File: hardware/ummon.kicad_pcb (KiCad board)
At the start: 4 copper layers, 140 x 83.5 mm, 85 parts, among them J1 Conn_01x08_Pin, J2 Conn_01x05_Pin, J3 Conn_01x04_Pin, J4 Conn_01x04_Pin, J5 Conn_01x04_Pin, P1 FPC 0.5MM 24P Vertical, Q1 SI1308EDL, SW1 Reboot, SW2 Flash, SW3 Test Button, U1 ESP32-C6-WROOM-1-N8, U2 SCD41-D-R2, U3 SGP41-D-R4, U4 SHT41-AD1B-R2, U5 AMS1117-3.3, U7 SMBJ6.5CA

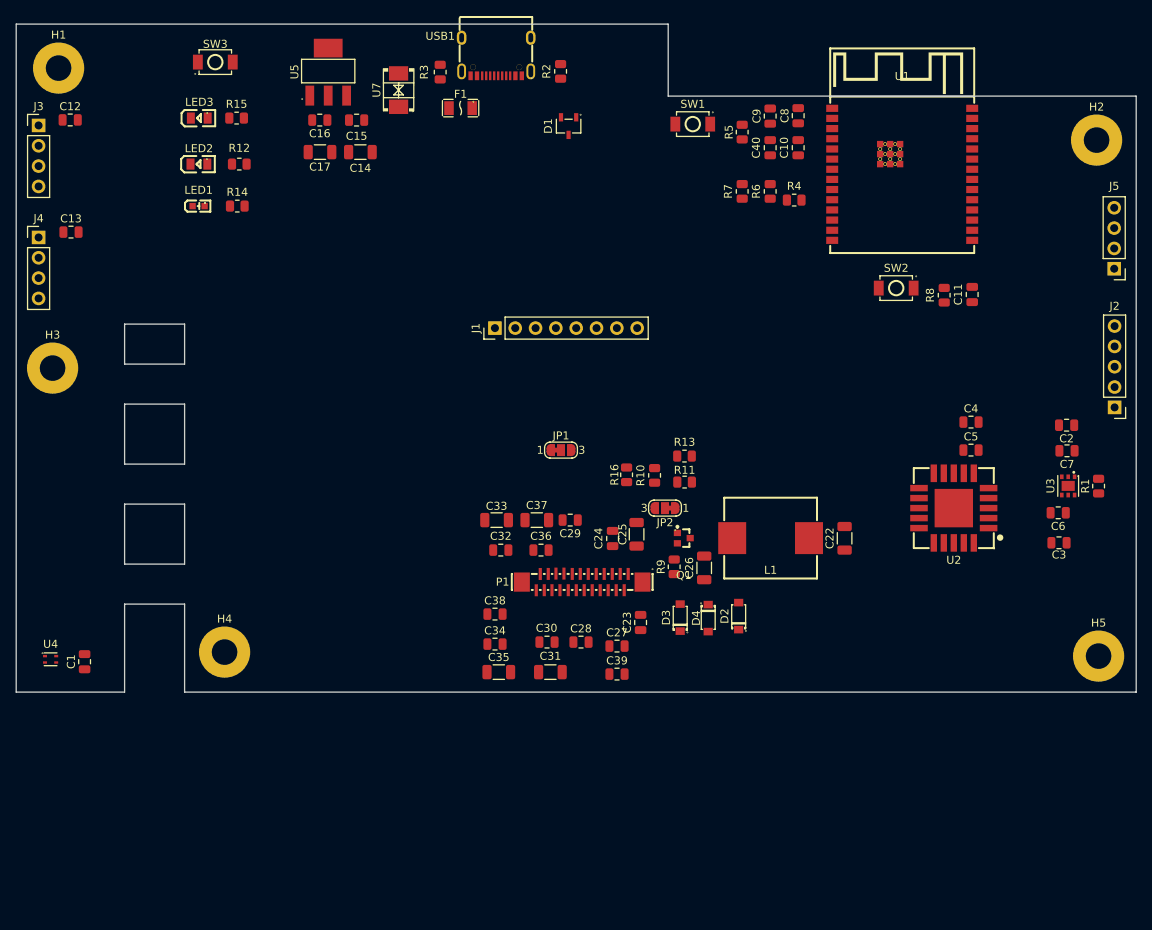
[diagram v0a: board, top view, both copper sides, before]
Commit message: :recycle: Propper outline of pcb and rearangement
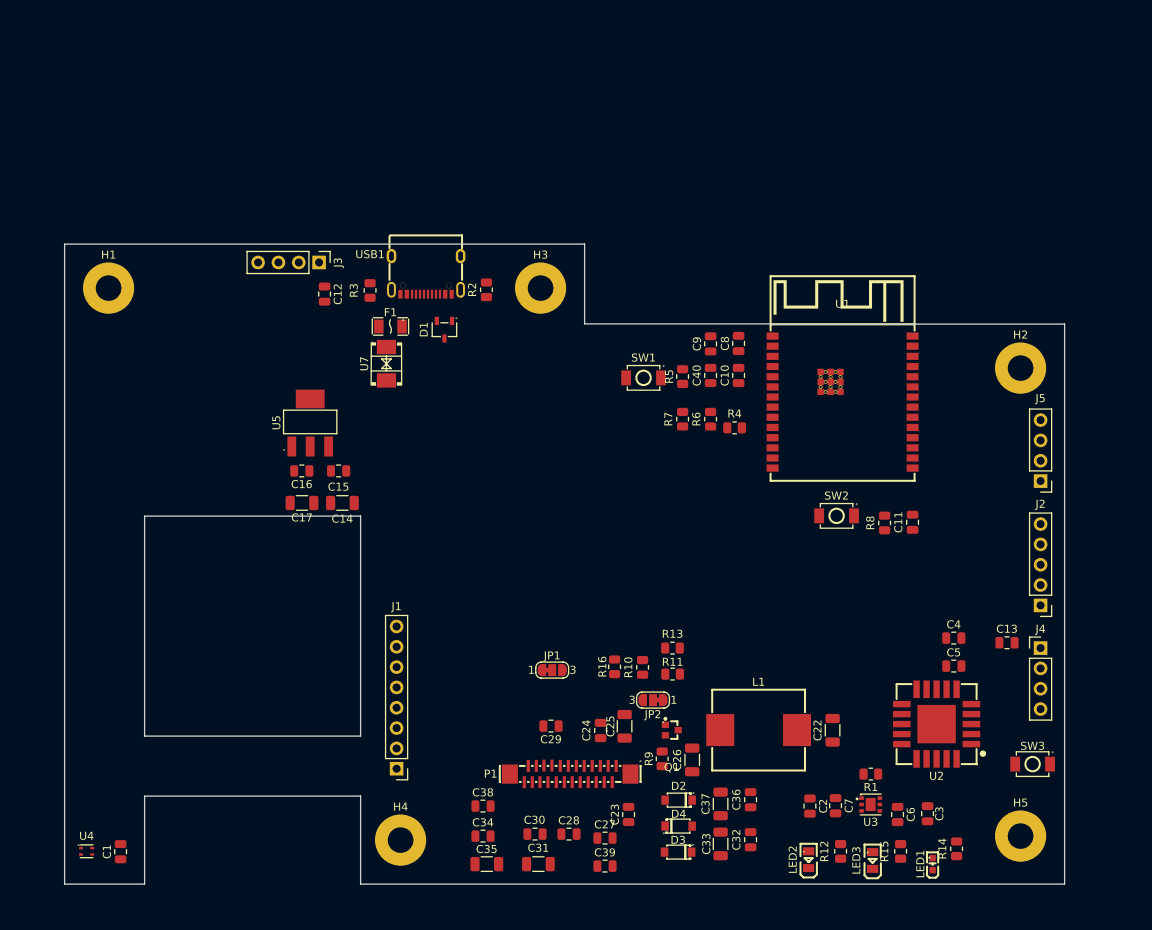
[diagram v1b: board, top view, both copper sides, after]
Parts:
- moved J4 135.4 mm to (172.0, 120.5)
- moved SW3 134.7 mm to (171.0, 135.0), turned to 0 degrees
- moved C13 127.8 mm to (167.8, 119.8), turned to 180 degrees
- moved LED3 125.3 mm to (151.0, 147.1), turned to 90 degrees
- moved R15 123.7 mm to (154.5, 145.9), turned to 90 degrees
- moved LED1 123.2 mm to (158.5, 147.5), turned to 90 degrees
- moved R14 120.6 mm to (161.5, 145.6), turned to -90 degrees
- moved LED2 115.6 mm to (143.0, 146.9), turned to 90 degrees
- moved R12 114.2 mm to (147.0, 145.9), turned to 90 degrees
- moved H3 61.8 mm to (109.5, 75.5)
- moved C2 57.4 mm to (143.2, 140.2), turned to -90 degrees
- moved J1 56.4 mm to (91.5, 135.6), turned to 180 degrees
- moved C7 53.0 mm to (146.4, 140.2), turned to -90 degrees
- moved C33 49.2 mm to (132.0, 145.0), turned to -90 degrees
- moved C32 47.8 mm to (135.8, 144.4), turned to -90 degrees
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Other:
- board size 140 x 83.5 mm -> 125 x 80 mm

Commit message: :sparkles: Rounding of pcb edges
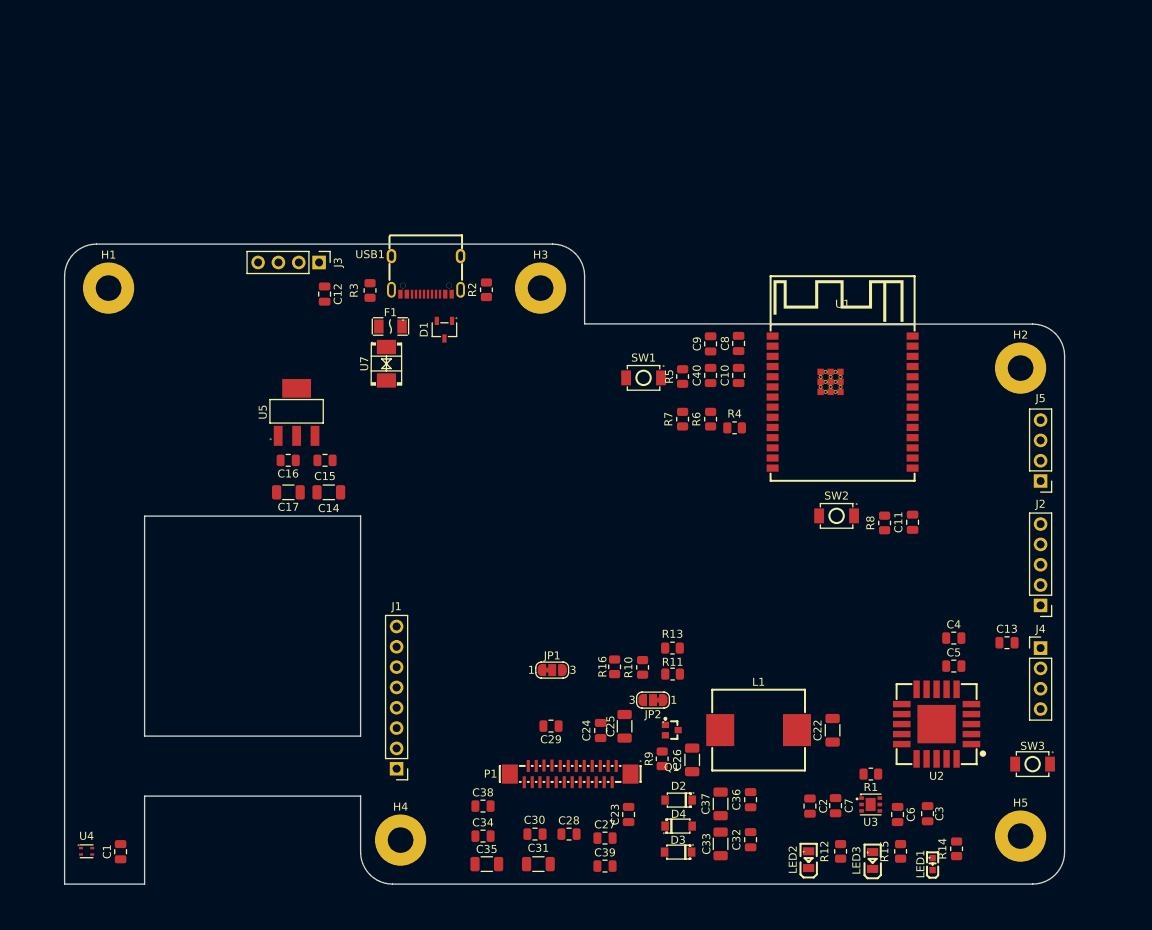
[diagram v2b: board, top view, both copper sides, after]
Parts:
- moved C15 2.16 mm to (82.5, 97.0)
- moved C16 2.16 mm to (78.0, 97.0)
- moved C17 2.16 mm to (78.0, 101.0)
- moved U5 2.16 mm to (79.0, 91.0)
- moved C14 2.16 mm to (83.0, 101.0)
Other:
- outline, holes or cut-outs redrawn
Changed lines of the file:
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@@
 	(footprint "Capacitor_SMD:C_0805_2012Metric"
 		(layer "F.Cu")
-		(at 79.65 98.3575 180)
+		(at 77.95 97.03 180)
 		(descr "Capacitor SMD 0805 (2012 Metric), square (rectangular) end terminal, IPC-7351 nominal, (Body size source: IPC-SM-782 page 76, https://www.pcb-3d.com/wordpress/wp-content/uploads/ipc-sm-782a_amendment_1_and_2.pdf, https://docs.google.com/spreadsheets/d/1BsfQQcO9C6DZCsRaXUlFlo91Tg2WpOkGARC1WS5S8t0/edit?usp=sharing)")
 		(tags "capacitor")
@@
 	(footprint "Capacitor_SMD:C_0805_2012Metric"
 		(layer "F.Cu")
-		(at 84.25 98.3575)
+		(at 82.55 97.03)
 		(descr "Capacitor SMD 0805 (2012 Metric), square (rectangular) end terminal, IPC-7351 nominal, (Body size source: IPC-SM-782 page 76, https://www.pcb-3d.com/wordpress/wp-content/uploads/ipc-sm-782a_amendment_1_and_2.pdf, https://docs.google.com/spreadsheets/d/1BsfQQcO9C6DZCsRaXUlFlo91Tg2WpOkGARC1WS5S8t0/edit?usp=sharing)")
 		(tags "capacitor")
@@
 	(footprint "parts:SOT-223-3_L6.5-W3.4-P2.30-LS7.0-BR"
 		(layer "F.Cu")
-		(at 80.7 92.3275 -90)
+		(at 79 91 -90)
 		(property "Reference" "U5"
 			(at 0 4.2 90)
@@
 	(footprint "Capacitor_SMD:C_1206_3216Metric"
 		(layer "F.Cu")
-		(at 84.725 102.3575)
+		(at 83.025 101.03)
 		(descr "Capacitor SMD 1206 (3216 Metric), square (rectangular) end terminal, IPC-7351 nominal, (Body size source: IPC-SM-782 page 76, https://www.pcb-3d.com/wordpress/wp-content/uploads/ipc-sm-782a_amendment_1_and_2.pdf)")
 		(tags "capacitor")
@@
 	(footprint "Capacitor_SMD:C_1206_3216Metric"
 		(layer "F.Cu")
-		(at 79.675 102.3575 180)
+		(at 77.975 101.03 180)
 		(descr "Capacitor SMD 1206 (3216 Metric), square (rectangular) end terminal, IPC-7351 nominal, (Body size source: IPC-SM-782 page 76, https://www.pcb-3d.com/wordpress/wp-content/uploads/ipc-sm-782a_amendment_1_and_2.pdf)")
 		(tags "capacitor")
@@
 		)
 	)
+	(gr_arc
+		(start 50 74)
+		(mid 51.171573 71.171573)
+		(end 54 70)
+		(stroke
+			(width 0.05)
+			(type default)
+		)
+		(layer "Edge.Cuts")
+	)
 	(gr_line
 		(start 50 150)
-		(end 50 70)
+		(end 50 74)
 		(stroke
 			(width 0.05)
@@
 	)
 	(gr_line
-		(start 87 150)
+		(start 87 146)
 		(end 87 139)
 		(stroke
@@
 		(layer "Edge.Cuts")
 	)
+	(gr_arc
+		(start 91 150)
+		(mid 88.171573 148.828427)
+		(end 87 146)
+		(stroke
+			(width 0.05)
+			(type default)
+		)
+		(layer "Edge.Cuts")
+	)
 	(gr_line
-		(start 87 150)
-		(end 175 150)
+		(start 91 150)
+		(end 171 150)
 		(stroke
 			(width 0.05)
@@
 	)
 	(gr_line
-		(start 115 70)
-		(end 50 70)
+		(start 111 70)
+		(end 54 70)
+		(stroke
+			(width 0.05)
+			(type default)
+		)
+		(layer "Edge.Cuts")
+	)
+	(gr_arc
+		(start 111 70)
+		(mid 113.828427 71.171573)
+		(end 115 74)
 		(stroke
 			(width 0.05)
@@
 	(gr_line
 		(start 115 79.97)
-		(end 115 70)
+		(end 115 74)
 		(stroke
 			(width 0.05)
@@
 	)
 	(gr_line
-		(start 175 80)
+		(start 171.002 79.998001)
 		(end 115 79.97)
 		(stroke
@@
 		(layer "Edge.Cuts")
 	)
+	(gr_arc
+		(start 171.002 79.998001)
+		(mid 173.829134 81.17028)
+		(end 175 83.998)
+		(stroke
+			(width 0.05)
+			(type default)
+		)
+		(layer "Edge.Cuts")
+	)
+	(gr_arc
+		(start 175 146)
+		(mid 173.828427 148.828427)
+		(end 171 150)
+		(stroke
+			(width 0.05)
+			(type default)
+		)
+		(layer "Edge.Cuts")
+	)
 	(gr_line
-		(start 175 150)
-		(end 175 80)
+		(start 175 146)
+		(end 175 83.998)
 		(stroke
 			(width 0.05)

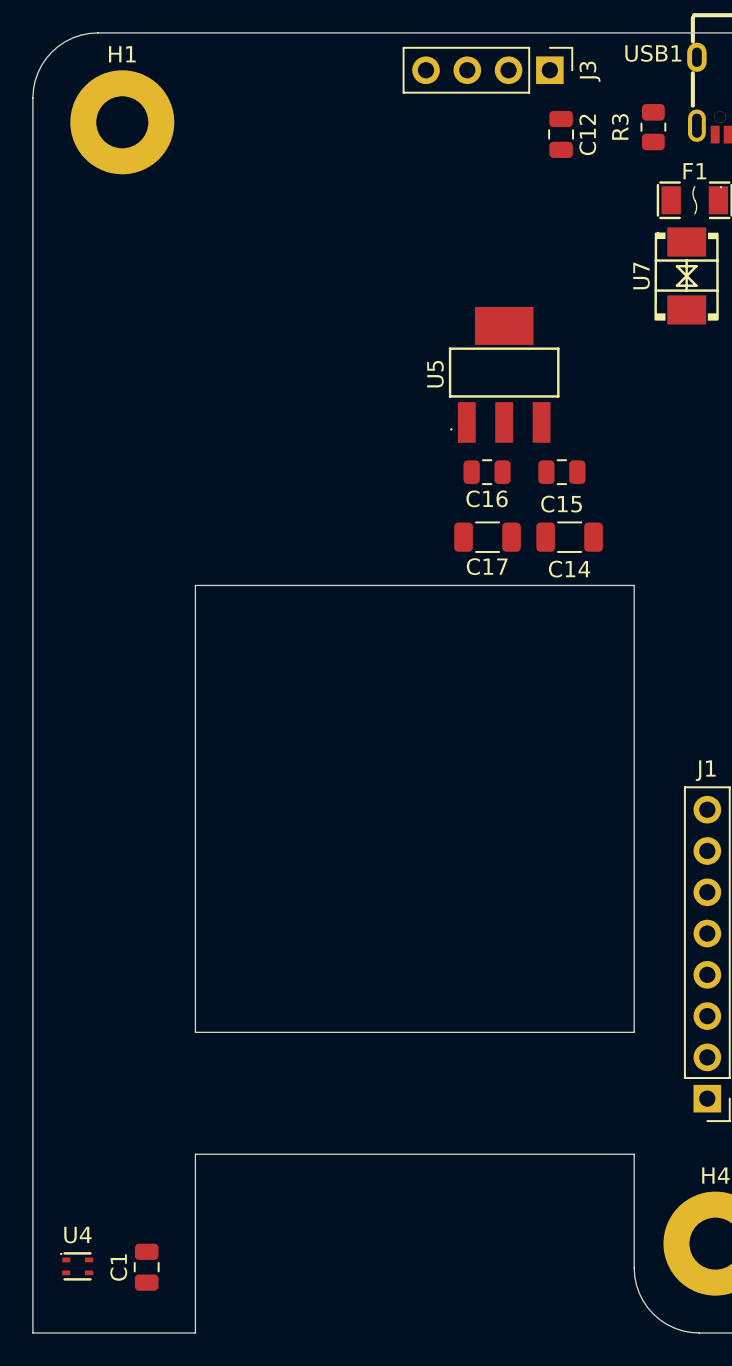
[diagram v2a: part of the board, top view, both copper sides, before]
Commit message: :sparkles: Add extra mounting hole for pcb sht41 part
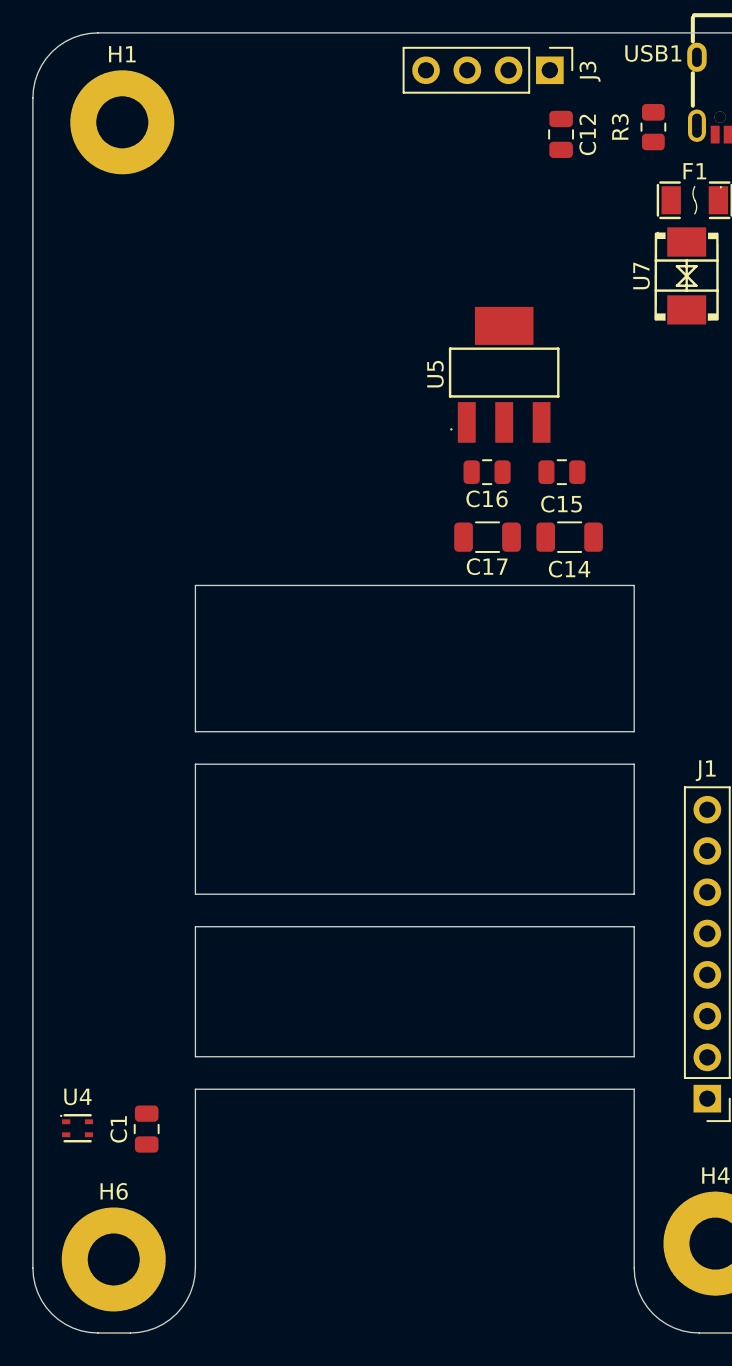
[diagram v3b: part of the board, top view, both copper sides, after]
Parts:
- added H6: MountingHole_Pad, MountingHole:MountingHole_3.2mm_M3_Pad, F.Cu at (55.0, 145.5)
- moved C1 8.50 mm to (57.0, 137.4)
- moved U4 8.50 mm to (52.8, 137.4)
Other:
- outline, holes or cut-outs redrawn
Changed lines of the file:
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@@
 	(footprint "Capacitor_SMD:C_0805_2012Metric"
 		(layer "F.Cu")
-		(at 57 145.95 90)
+		(at 57 137.45 90)
 		(descr "Capacitor SMD 0805 (2012 Metric), square (rectangular) end terminal, IPC-7351 nominal, (Body size source: IPC-SM-782 page 76, https://www.pcb-3d.com/wordpress/wp-content/uploads/ipc-sm-782a_amendment_1_and_2.pdf, https://docs.google.com/spreadsheets/d/1BsfQQcO9C6DZCsRaXUlFlo91Tg2WpOkGARC1WS5S8t0/edit?usp=sharing)")
 		(tags "capacitor")
@@
 	(footprint "parts:DFN-4_L1.5-W1.5-SHT41-AD1B-R2"
 		(layer "F.Cu")
-		(at 52.75 145.9)
+		(at 52.75 137.4)
 		(property "Reference" "U4"
 			(at 0 -1.9 0)
@@
 		(embedded_fonts no)
 	)
+	(footprint "MountingHole:MountingHole_3.2mm_M3_Pad"
+		(layer "F.Cu")
+		(at 54.975 145.475)
+		(descr "Mounting Hole 3.2mm, M3, generated by kicad-footprint-generator mountinghole.py")
+		(tags "mountinghole M3")
+		(property "Reference" "H6"
+			(at 0 -4.15 0)
+			(layer "F.SilkS")
+			(effects
+				(font
+					(size 1 1)
+					(thickness 0.15)
+				)
+			)
+		)
+		(property "Value" "MountingHole_Pad"
+			(at 0 4.15 0)
+			(layer "F.Fab")
+			(effects
+				(font
+					(size 1 1)
+					(thickness 0.15)
+				)
+			)
+		)
+		(property "Datasheet" ""
+			(at 0 0 0)
+			(layer "F.Fab")
+			(hide yes)
+			(effects
+				(font
+					(size 1.27 1.27)
+				)
+			)
+		)
+		(property "Description" "Mounting Hole with connection"
+			(at 0 0 0)
+			(layer "F.Fab")
+			(hide yes)
+			(effects
+				(font
+					(size 1.27 1.27)
+				)
+			)
+		)
+		(property "KiLib_Generator" "mounting_hardware/mounting_hole"
+			(at 0 0 0)
+			(layer "F.SilkS")
+			(hide yes)
+			(effects
+				(font
+					(size 1 1)
+					(thickness 0.15)
+				)
+			)
+		)
+		(property ki_fp_filters "MountingHole*Pad*")
+		(sheetname "/")
+		(sheetfile "ummon.kicad_sch")
+		(units
+			(unit
+				(name "A")
+				(pins "1")
+			)
+		)
+		(attr exclude_from_bom)
+		(duplicate_pad_numbers_are_jumpers no)
+		(fp_circle
+			(center 0 0)
+			(end 3.2 0)
+			(stroke
+				(width 0.15)
+				(type solid)
+			)
+			(fill no)
+			(layer "Cmts.User")
+		)
+		(fp_circle
+			(center 0 0)
+			(end 3.45 0)
+			(stroke
+				(width 0.05)
+				(type solid)
+			)
+			(fill no)
+			(layer "F.CrtYd")
+		)
+		(fp_text user "${REFERENCE}"
+			(at 0 0 0)
+			(layer "F.Fab")
+			(effects
+				(font
+					(size 1 1)
+					(thickness 0.15)
+				)
+			)
+		)
+		(pad "1" thru_hole circle
+			(at 0 0)
+			(size 6.4 6.4)
+			(drill 3.2)
+			(layers "*.Cu" "*.Mask")
+			(remove_unused_layers no)
+			(net "GND")
+			(pinfunction "1_1")
+			(pintype "input")
+			(zone_connect 2)
+		)
+		(embedded_fonts no)
+	)
 	(footprint "Capacitor_SMD:C_0805_2012Metric"
 		(layer "F.Cu")
@@
 	)
 	(gr_line
-		(start 50 150)
+		(start 50 146)
 		(end 50 74)
 		(stroke
@@
 		(layer "Edge.Cuts")
 	)
+	(gr_arc
+		(start 54 150)
+		(mid 51.171573 148.828427)
+		(end 50 146)
+		(stroke
+			(width 0.05)
+			(type default)
+		)
+		(layer "Edge.Cuts")
+	)
+	(gr_line
+		(start 56 150)
+		(end 54 150)
+		(stroke
+			(width 0.05)
+			(type default)
+		)
+		(layer "Edge.Cuts")
+	)
 	(gr_line
 		(start 60 104)
-		(end 60 131.5)
+		(end 60 113)
+		(stroke
+			(width 0.05)
+			(type default)
+		)
+		(layer "Edge.Cuts")
+	)
+	(gr_line
+		(start 60 115)
+		(end 60 123)
 		(stroke
 			(width 0.05)
@@
 	)
 	(gr_line
-		(start 60 139)
-		(end 60 150)
+		(start 60 125)
+		(end 60 133)
 		(stroke
 			(width 0.05)
@@
 	)
 	(gr_line
-		(start 60 150)
-		(end 50 150)
+		(start 60 135)
+		(end 60 146)
+		(stroke
+			(width 0.05)
+			(type default)
+		)
+		(layer "Edge.Cuts")
+	)
+	(gr_arc
+		(start 60 146)
+		(mid 58.828427 148.828427)
+		(end 56 150)
 		(stroke
 			(width 0.05)
@@
 	(gr_line
 		(start 87 104)
-		(end 87 131.5)
+		(end 87 113)
+		(stroke
+			(width 0.05)
+			(type default)
+		)
+		(layer "Edge.Cuts")
+	)
+	(gr_line
+		(start 87 113)
+		(end 60 113)
+		(stroke
+			(width 0.05)
+			(type default)
+		)
+		(layer "Edge.Cuts")
+	)
+	(gr_line
+		(start 87 115)
+		(end 60 115)
+		(stroke
+			(width 0.05)
+			(type default)
+		)
+		(layer "Edge.Cuts")
+	)
+	(gr_line
+		(start 87 115)
+		(end 87 123)
+		(stroke
+			(width 0.05)
+			(type default)
+		)
+		(layer "Edge.Cuts")
+	)
+	(gr_line
+		(start 87 123)
+		(end 60 123)
+		(stroke
+			(width 0.05)
+			(type default)
+		)
+		(layer "Edge.Cuts")
+	)
+	(gr_line
+		(start 87 125)
+		(end 60 125)
+		(stroke
+			(width 0.05)
+			(type default)
+		)
+		(layer "Edge.Cuts")
+	)
+	(gr_line
+		(start 87 133)
+		(end 60 133)
 		(stroke
 			(width 0.05)
@@
 	)
 	(gr_line
-		(start 87 131.5)
-		(end 60 131.5)
+		(start 87 133)
+		(end 87 125)
 		(stroke
 			(width 0.05)
@@
 	)
 	(gr_line
-		(start 87 139)
-		(end 60 139)
+		(start 87 135)
+		(end 60 135)
 		(stroke
 			(width 0.05)
@@
 	(gr_line
 		(start 87 146)
-		(end 87 139)
+		(end 87 135)
 		(stroke
 			(width 0.05)
